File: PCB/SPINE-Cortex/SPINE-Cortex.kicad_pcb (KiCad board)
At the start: 2 copper layers, 49 x 49 mm, 78 parts, among them J1 SWD, J2 Conn_01x08, J3 Conn_01x02, J4 CAN_IN, J5 CAN_OUT, U1 STM32F103C8Tx, U4 MIC5219-3.3YM5, U5 TCAN1044V, U7 TPS54240DGQ, Y1 Resonator

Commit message: Finish Vertebra
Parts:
- removed C6: 100nF, Capacitor_SMD:C_0603_1608Metric
- removed J3: Conn_01x02, Connector_PinHeader_2.00mm:PinHeader_1x02_P2.00mm_Vertical
- removed R17: 10K, Resistor_SMD:R_0603_1608Metric
- added C1: 100nF, Capacitor_SMD:C_0603_1608Metric, F.Cu at (93.1, 117.6)
- added R16: 120R, Resistor_SMD:R_0603_1608Metric, F.Cu at (90.1, 117.6)
- added U3: SP3485EN, Package_SO:SOIC-8_3.9x4.9mm_P1.27mm, F.Cu at (90.1, 113.1)
- J2: value Conn_01x08 -> Conn_01x06; footprint Connector_JST:JST_GH_SM08B-GHS-TB_1x08-1MP_P1.25mm_Horizontal -> Connector_JST:JST_GH_SM06B-GHS-TB_1x06-1MP_P1.25mm_Horizontal
- U1: value STM32F103C8Tx -> STM32G431RBTx; footprint Package_QFP:LQFP-48_7x7mm_P0.5mm -> Package_QFP:LQFP-64_10x10mm_P0.5mm
- moved C16 58.4 mm to (99.6, 108.0)
- moved U4 58.4 mm to (96.0, 107.2)
- moved C17 55.7 mm to (99.6, 106.3), turned to 0 degrees
- moved C8 50.4 mm to (82.5, 104.2)
- moved D4 50.4 mm to (79.0, 101.4)
- moved R1 50.4 mm to (82.5, 102.7)
- moved R15 50.4 mm to (92.5, 102.2)
- moved R2 50.4 mm to (82.5, 101.2)
- moved R3 50.4 mm to (85.5, 104.2)
- moved R4 50.4 mm to (91.5, 104.2)
- moved R5 50.4 mm to (88.5, 104.2)
- moved C14 50.4 mm to (92.5, 100.6)
- moved C2 50.4 mm to (84.4, 97.6)
- moved C11 50.4 mm to (94.8, 101.4)
- moved C15 50.4 mm to (87.7, 98.8)
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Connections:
- J2 pad 1: unconnected-(J2-Pin_1-Pad1) -> GND
- J2 pad 2: unconnected-(J2-Pin_2-Pad2) -> +5V
- J2 pad 3: unconnected-(J2-Pin_3-Pad3) -> RS485_A
- J2 pad 4: unconnected-(J2-Pin_4-Pad4) -> RS485_B
- J2 pad 5: unconnected-(J2-Pin_5-Pad5) -> FAULT
- J2 pad 6: unconnected-(J2-Pin_6-Pad6) -> ENABLE
- U1 pad 15: unconnected-(U1-PA5-Pad15) -> GND
- U1 pad 16: unconnected-(U1-PA6-Pad16) -> +3.3V
- U1 pad 23: GND -> unconnected-(U1-PC5-Pad23)
- U1 pad 24: +3.3V -> unconnected-(U1-PB0-Pad24)
- U1 pad 27: unconnected-(U1-PB14-Pad27) -> GND
- U1 pad 28: unconnected-(U1-PB15-Pad28) -> Reset
- U1 pad 29: unconnected-(U1-PA8-Pad29) -> VREF
- U1 pad 31: unconnected-(U1-PA10-Pad31) -> GND
- U1 pad 32: CANRX -> +3.3V
- U1 pad 33: CANTX -> unconnected-(U1-PB11-Pad33)
- U1 pad 34: SWDIO -> unconnected-(U1-PB12-Pad34)
- U1 pad 35: GND -> unconnected-(U1-PB13-Pad35)
- U1 pad 36: +3.3V -> unconnected-(U1-PB14-Pad36)
- U1 pad 37: SWCLK -> unconnected-(U1-PB15-Pad37)
- U1 pad 44: BOOT -> unconnected-(U1-PA10-Pad44)
- U1 pad 45: unconnected-(U1-PB8-Pad45) -> CANRX
- U1 pad 46: unconnected-(U1-PB9-Pad46) -> CANTX
- U1 pad 7: Reset -> BOOT
- U1 pad 8: GND -> unconnected-(U1-PC0-Pad8)
- U1 pad 9: VREF -> unconnected-(U1-PC1-Pad9)
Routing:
- added copper zone on B.Cu, net GND

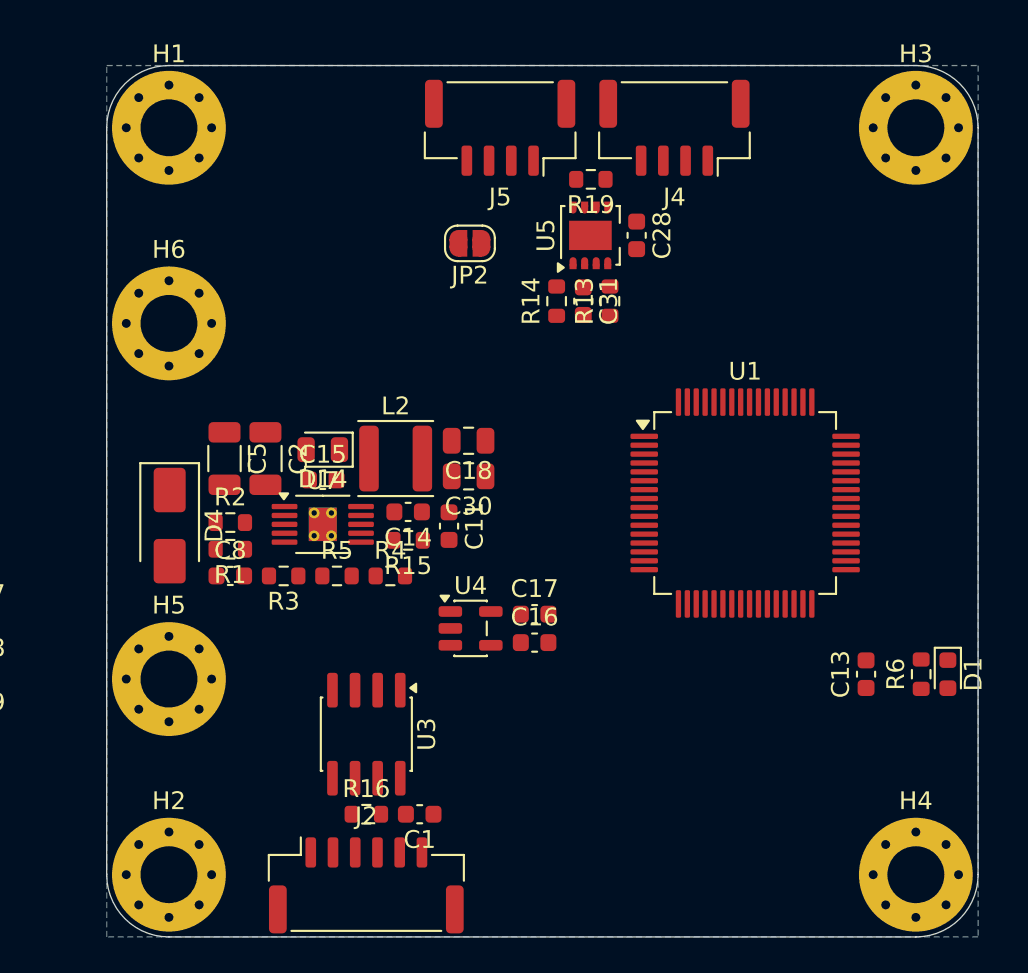
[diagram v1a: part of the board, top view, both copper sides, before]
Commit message: Vertebra fix
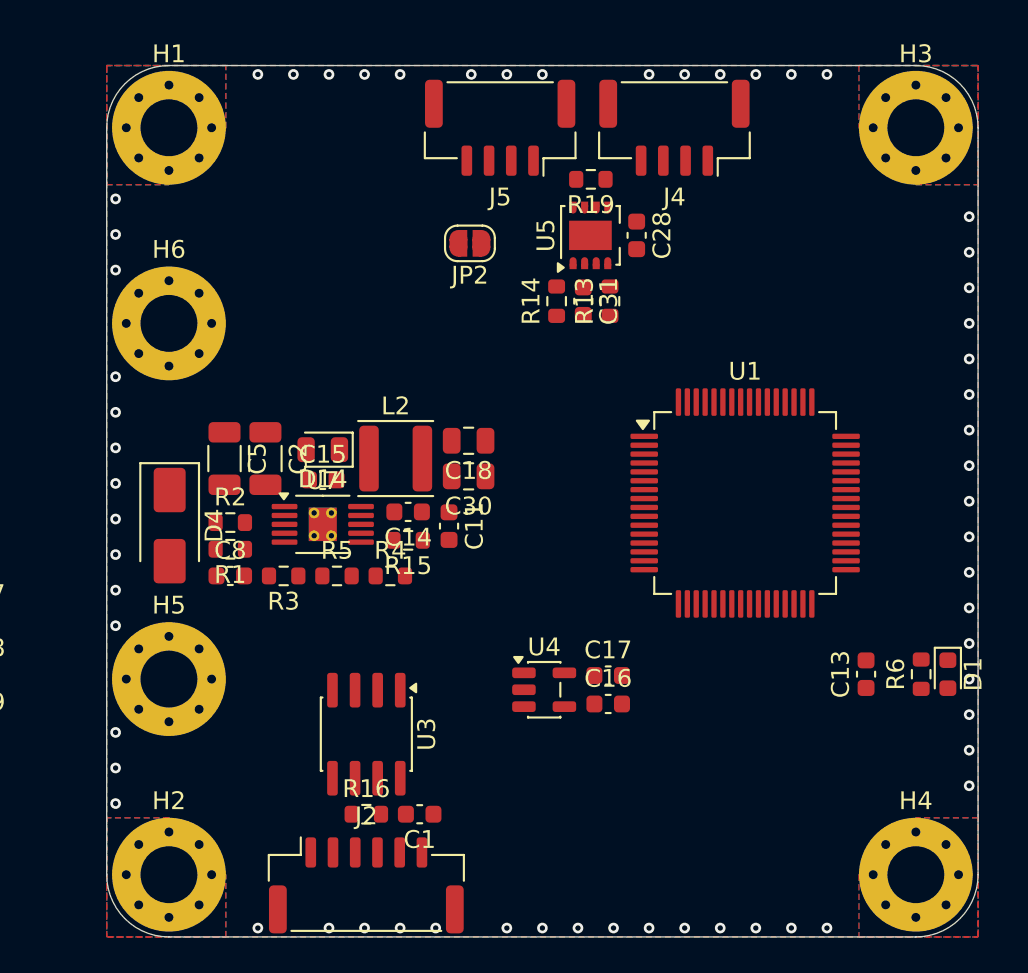
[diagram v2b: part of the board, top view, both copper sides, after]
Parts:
- moved C16 5.39 mm to (103.7, 111.4)
- moved C17 5.39 mm to (103.7, 109.8)
- moved U4 5.39 mm to (100.1, 110.6)
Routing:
- net GND: vias 0 -> 60
- added copper zone on F.Cu, net GND
- added copper zone on B.Cu, net unconnected-(H1-Pad1)
- added copper zone on F.Cu, net unconnected-(H1-Pad1)
- added copper zone on B.Cu, net unconnected-(H2-Pad1)
- added copper zone on F.Cu, net unconnected-(H2-Pad1)
- added copper zone on B.Cu, net unconnected-(H3-Pad1)
- added copper zone on F.Cu, net unconnected-(H3-Pad1)
- added copper zone on B.Cu, net unconnected-(H4-Pad1)
- added copper zone on F.Cu, net unconnected-(H4-Pad1)

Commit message: update
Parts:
- removed C4: 100nF, Capacitor_SMD:C_0603_1608Metric
- removed C45: 10uF, Capacitor_SMD:C_1206_3216Metric
- removed TH1: Thermistor_NTC, Resistor_SMD:R_0603_1608Metric
- added BZ1: Buzzer, Buzzer_Beeper:Buzzer_12x9.5RM7.6, F.Cu at (56.7, 82.0)
- added C3: 100nF, Capacitor_SMD:C_0603_1608Metric, F.Cu at (116.1, 111.8)
- added C6: 100nF, Capacitor_SMD:C_0603_1608Metric, F.Cu at (120.9, 107.9)
- added D2: B5819WS, Diode_SMD:D_0805_2012Metric, F.Cu at (57.0, 90.3)
- added D3: WS2812B-2020, LED_SMD:LED_WS2812B-2020_PLCC4_2.0x2.0mm, F.Cu at (110.6, 78.5)
- added J3: Conn_01x02, Connector_PinHeader_2.00mm:PinHeader_1x02_P2.00mm_Vertical, F.Cu at (121.6, 112.8)
- added J6: CAN_IN, Connector_JST:JST_GH_SM04B-GHS-TB_1x04-1MP_P1.25mm_Horizontal, F.Cu at (118.2, 58.0)
- added J7: Conn_01x02, TerminalBlock_MetzConnect:TerminalBlock_MetzConnect_Type094_RT03502HBLU_1x02_P5.00mm_Horizontal, F.Cu at (119.7, 85.9)
- added Q1: Q_NMOS_GSD, Package_TO_SOT_SMD:SOT-23, F.Cu at (61.0, 90.3)
- added Q2: Q_NMOS_GSD, Package_TO_SOT_SMD:SOT-23, F.Cu at (110.5, 56.5)
- added Q3: Q_NMOS_GSD, Package_TO_SOT_SMD:SOT-23, F.Cu at (110.5, 61.0)
- added Q4: Q_NMOS_GSD, Package_TO_SOT_SMD:SOT-23, F.Cu at (110.5, 65.5)
- added Q7: Q_PMOS_GSD, Package_TO_SOT_SMD:SOT-23, F.Cu at (107.2, 120.0)
- added Q8: Q_NMOS_GSD, Package_TO_SOT_SMD:SOT-23, F.Cu at (110.4, 118.2)
- added R17: 10K, Resistor_SMD:R_0603_1608Metric, F.Cu at (63.7, 90.3)
- added R18: 10K, Resistor_SMD:R_0603_1608Metric, F.Cu at (112.9, 120.2)
- added R20: 10K, Resistor_SMD:R_0603_1608Metric, F.Cu at (66.4, 91.1)
- added R21: 1K, Resistor_SMD:R_0603_1608Metric, F.Cu at (108.6, 92.8)
- added R22: 10K, Resistor_SMD:R_0603_1608Metric, F.Cu at (107.2, 117.3)
- added R23: 220R, Resistor_SMD:R_0603_1608Metric, F.Cu at (108.7, 84.4)
- added R24: 1K, Resistor_SMD:R_0603_1608Metric, F.Cu at (103.8, 117.6)
- added R26: 10K, Resistor_SMD:R_0603_1608Metric, F.Cu at (110.4, 120.9)
- added U2: STM32G431RBTx, Package_QFP:LQFP-64_10x10mm_P0.5mm, F.Cu at (110.4, 105.8)
- U1: value STM32G431RBTx -> SFH617A-2X009T; footprint Package_QFP:LQFP-64_10x10mm_P0.5mm -> Package_DIP:SMDIP-4_W9.53mm_Clearance8mm
- moved C7 74.9 mm to (111.1, 114.1), turned to 90 degrees
- moved C23 74.2 mm to (116.4, 100.1), turned to 90 degrees
- moved C9 72.4 mm to (109.6, 114.1), turned to 90 degrees
- moved R10 71.0 mm to (120.9, 109.4)
- moved FB1 69.2 mm to (113.4, 113.3), turned to 180 degrees
- moved Y1 68.3 mm to (101.4, 103.8), turned to -90 degrees
- moved C26 63.3 mm to (104.7, 98.3), turned to 180 degrees
- moved C21 62.9 mm to (104.4, 111.5), turned to -90 degrees
- moved J1 62.8 mm to (121.4, 104.6), turned to 180 degrees
- moved C24 62.8 mm to (104.7, 99.8), turned to 180 degrees
- moved C19 59.8 mm to (101.4, 108.3)
- moved R9 57.4 mm to (107.7, 98.3)
- moved R7 52.7 mm to (101.4, 106.8), turned to 180 degrees
- moved C18 48.5 mm to (48.8, 108.6), turned to -90 degrees
- moved C34 47.3 mm to (79.0, 95.4)
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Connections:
- C2 pad 2: Net-(D4-K) -> VDC
- C5 pad 2: Net-(D4-K) -> VDC
- D4 pad 1: Net-(D4-K) -> VDC
- D4 pad 2: VDC -> PRI_HI
- H5 pad 1: VDC -> PRI_HI
- J2 pad 5: FAULT -> ENABLE
- J2 pad 6: ENABLE -> FAULT
- R2 pad 2: Net-(D4-K) -> VDC
- U1 pad 1: +3.3V -> Net-(J7-Pin_1)
- U1 pad 2: unconnected-(U1-PC13-Pad2) -> Net-(R23-Pad1)
- U1 pad 3: unconnected-(U1-PC14-Pad3) -> TIM_BKIN_1
- U1 pad 4: unconnected-(U1-PC15-Pad4) -> +3.3V
- U7 pad 2: Net-(D4-K) -> VDC
- Y1 pad 1: Net-(U1-PF0) -> Net-(U2-PF0)
- Y1 pad 3: Net-(U1-PF1) -> Net-(U2-PF1)
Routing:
- net Net-(J7-Pin_1): track 0.00 -> 6.96 mm
- net Net-(Q7-G): track 0.00 -> 4.20 mm
- net +5V: track 0.00 -> 1.81 mm
- net Net-(Q8-G): track 0.00 -> 1.81 mm
- net GND: vias 60 -> 58

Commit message: update
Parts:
- removed C43, C44: 10uF, Capacitor_SMD:C_1206_3216Metric
- removed D6: LED_RBAG, LED_SMD:LED_Cree-PLCC4_2x2mm_CW
- removed J1: SWD, Connector_PinHeader_2.54mm:PinHeader_1x03_P2.54mm_Vertical
- removed Q2, Q3, Q4: Q_NMOS_GSD, Package_TO_SOT_SMD:SOT-23
- removed R11, R12, R8: 1K, Resistor_SMD:R_0603_1608Metric
- added C4: 100nF, Capacitor_SMD:C_0603_1608Metric, F.Cu at (84.9, 109.4)
- added D5: LED_Small, LED_SMD:LED_0603_1608Metric, F.Cu at (83.3, 123.0)
- added D7: B5819WS, Diode_SMD:D_0805_2012Metric, F.Cu at (88.2, 87.1)
- added J9: Conn_02x03_Odd_Even, Connector_PinHeader_2.54mm:PinHeader_2x03_P2.54mm_Vertical, F.Cu at (103.5, 119.3)
- added R25: 1K, Resistor_SMD:R_0603_1608Metric, F.Cu at (83.3, 120.0)
- BZ1: footprint Buzzer_Beeper:Buzzer_12x9.5RM7.6 -> Buzzer_Beeper:MagneticBuzzer_CUI_CMT-8504-100-SMT
- J3: footprint Connector_PinHeader_2.00mm:PinHeader_1x02_P2.00mm_Vertical -> Connector_PinHeader_2.54mm:PinHeader_1x02_P2.54mm_Vertical
- moved J6 78.7 mm to (98.7, 134.3)
- moved J5 76.2 mm to (120.4, 131.6), turned to 0 degrees
- moved U3 74.3 mm to (137.3, 118.9)
- moved C1 74.3 mm to (140.8, 121.1)
- moved R16 73.4 mm to (137.3, 123.4)
- moved J4 70.2 mm to (110.9, 131.6), turned to 0 degrees
- moved TP1 66.4 mm to (110.3, 60.6)
- moved TP2 66.4 mm to (110.3, 63.6)
- moved TP3 66.4 mm to (110.3, 66.7)
- moved TP4 66.4 mm to (113.3, 60.6)
- moved TP5 66.4 mm to (113.3, 63.6)
- moved TP6 66.4 mm to (113.3, 66.7)
- moved TP7 66.4 mm to (116.4, 60.6)
- moved TP8 66.4 mm to (116.4, 63.6)
- moved TP9 66.4 mm to (116.4, 66.7)
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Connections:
- BZ1 pad 1: +5V -> Net-(BZ1-+)
- D2 pad 1: +5V -> Net-(BZ1-+)
- D3 pad 2: unconnected-(D3-VSS-Pad2) -> GND
- D3 pad 3: unconnected-(D3-DIN-Pad3) -> LED1
- D3 pad 4: unconnected-(D3-VDD-Pad4) -> +5V
- R21 pad 2: TIM_BKIN_1 -> TIM_BKIN_2
- R6 pad 1: +3.3V -> +5V
- U1 pad 3: TIM_BKIN_1 -> TIM_BKIN_2
- U2 pad 13: unconnected-(U2-PA1-Pad13) -> USART2_DE
- U2 pad 14: unconnected-(U2-PA2-Pad14) -> USART2_TX
- U2 pad 17: unconnected-(U2-PA3-Pad17) -> USART2_RX
- U2 pad 20: unconnected-(U2-PA6-Pad20) -> FAULT
- U2 pad 59: unconnected-(U2-PB6-Pad59) -> TIM_BKIN_2
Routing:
- net VDC: track 0.00 -> 24.3 mm
- net +5V: track 1.81 -> 8.52 mm
- net VREF: track 0.00 -> 5.51 mm
- net PRI_HI: track 0.00 -> 5.50 mm
- net Net-(BZ1-+): track 0.00 -> 5.44 mm
- net +3.3V: track 0.00 -> 5.11 mm
- net Net-(U7-VSENSE): track 0.00 -> 4.96 mm
- net Net-(U7-EN): track 0.00 -> 4.93 mm
- net Net-(U7-COMP): track 0.00 -> 3.79 mm
- net Net-(U7-RT/CLK): track 0.00 -> 3.21 mm
- net Net-(BZ1--): track 0.00 -> 2.92 mm
- net TIM_BKIN_2: track 0.00 -> 2.75 mm
- net Net-(U7-SS/TR): track 0.00 -> 2.54 mm
- net Net-(R23-Pad1): track 0.00 -> 2.44 mm
- net Net-(Q7-G): track 4.20 -> 1.81 mm
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- added copper zone on F.Cu, net +5V
- added copper zone on F.Cu, net Net-(D14-K)
- added copper zone on F.Cu, net Net-(U7-BOOT)
- added copper zone on F.Cu, net VDC
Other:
- board text added: "3V3"
- board text added: "CLK"
- board text added: "DIO"
- board text added: "GND"
- board text added: "RXD"
- board text added: "TXD"

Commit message: update
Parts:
- removed C13: 10uF, Capacitor_SMD:C_0603_1608Metric
- removed J9: Conn_02x03_Odd_Even, Connector_PinHeader_2.54mm:PinHeader_2x03_P2.54mm_Vertical
- added C10: 100nF, Capacitor_SMD:C_0603_1608Metric, F.Cu at (103.6, 117.2)
- added J1: Conn_01x02, Connector_PinHeader_2.54mm:PinHeader_1x02_P2.54mm_Vertical, F.Cu at (103.6, 122.4)
- added J8: Conn_01x03, Connector_PinHeader_2.54mm:PinHeader_1x03_P2.54mm_Vertical, B.Cu at (97.0, 95.5)
- added R8: 10K, Resistor_SMD:R_0603_1608Metric, F.Cu at (103.6, 115.7)
- added SW1: SW_Push, Button_Switch_SMD:SW_SPST_B3S-1000, F.Cu at (120.8, 93.0)
- added SW2: SW_Push, Button_Switch_SMD:SW_SPST_B3S-1000, F.Cu at (120.8, 103.5)
- moved J5 60.8 mm to (90.0, 79.0), turned to 180 degrees
- moved J4 53.7 mm to (100.0, 79.0), turned to 180 degrees
- moved R19 51.1 mm to (83.9, 80.6), turned to -90 degrees
- moved JP2 49.8 mm to (83.9, 77.4)
- moved U5 46.0 mm to (101.5, 86.0), turned to 90 degrees
- moved C28 44.4 mm to (104.1, 86.0), turned to -90 degrees
- moved R14 42.5 mm to (100.0, 89.8), turned to 90 degrees
- moved C31 41.4 mm to (101.5, 89.8), turned to -90 degrees
- moved R13 40.3 mm to (103.0, 89.8), turned to 90 degrees
- moved J3 39.8 mm to (99.9, 122.4)
- moved C6 36.2 mm to (99.9, 117.2), turned to 0 degrees
- moved R10 35.0 mm to (99.9, 115.7), turned to 0 degrees
- moved Q8 29.2 mm to (119.9, 111.8), turned to 180 degrees
- moved R16 29.1 mm to (109.1, 116.2), turned to 90 degrees
- moved R18 28.9 mm to (120.5, 109.3)
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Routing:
- net +5V: track 8.52 -> 135.5 mm, vias 0 -> 2
- net +3.3V: track 5.11 -> 67.9 mm
- net ENABLE: track 0.00 -> 15.2 mm
- net FAULT: track 0.00 -> 12.0 mm
- net USART2_DE: track 0.00 -> 11.2 mm
- net RS485_B: track 0.00 -> 9.43 mm
- net CAN_L: track 0.00 -> 9.21 mm
- net Net-(Q8-G): track 0.00 -> 8.31 mm
- net USART2_RX: track 0.00 -> 8.08 mm
- net CANTX: track 0.00 -> 7.92 mm
- net RS485_A: track 0.00 -> 6.67 mm
- net USART2_TX: track 0.00 -> 5.92 mm
- net CANRX: track 0.00 -> 5.80 mm
- net Reset: track 0.00 -> 5.72 mm
- net VREF: track 5.51 -> 0.00 mm
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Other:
- board text added: "BOOT"
- board text added: "NTC1"
- board text added: "NTC2"
- board text removed: "3V3"
- board text removed: "RXD"
- board text removed: "TXD"

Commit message: update
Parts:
- removed TP6: TestPoint, TestPoint:TestPoint_Pad_D1.0mm
- added C12: 100nF, Capacitor_SMD:C_0603_1608Metric, F.Cu at (88.3, 115.0)
- added R11: 147K, Resistor_SMD:R_0603_1608Metric, F.Cu at (86.7, 113.3)
- added R12: 10K, Resistor_SMD:R_0603_1608Metric, F.Cu at (89.9, 113.3)
- D1, D5: value LED_Small -> LED
- moved TP2 50.4 mm to (106.1, 113.9)
- moved TP4 49.5 mm to (96.2, 107.0)
- moved TP5 49.3 mm to (93.9, 109.0)
- moved TP1 49.2 mm to (93.9, 107.0)
- moved TP3 44.6 mm to (96.2, 109.0)
- moved TP7 35.2 mm to (106.1, 94.3)
- moved TP8 31.2 mm to (104.1, 92.3)
- moved TP9 30.2 mm to (104.0, 94.3)
- moved R24 11.6 mm to (113.0, 105.7), turned to -90 degrees
- moved R7 6.31 mm to (101.7, 113.7), turned to 180 degrees
- moved R10 1.13 mm to (99.1, 114.9), turned to 90 degrees
- moved R8 1.06 mm to (104.3, 114.9), turned to 90 degrees
- moved J4 0.60 mm to (100.0, 78.4)
- moved J5 0.60 mm to (90.0, 78.4)
- moved C21 0.42 mm to (111.5, 107.7), turned to -90 degrees
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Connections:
- D3 pad 1: unconnected-(D3-DOUT-Pad1) -> Net-(D3-DOUT)
- J6 pad 1: unconnected-(J6-Pin_1-Pad1) -> GND
- J6 pad 2: unconnected-(J6-Pin_2-Pad2) -> +5V
- J6 pad 3: unconnected-(J6-Pin_3-Pad3) -> LED1
- J6 pad 4: unconnected-(J6-Pin_4-Pad4) -> Net-(D3-DOUT)
- JP2 pad 1: CAN_L -> CAN_H
- R19 pad 2: CAN_H -> CAN_L
- SW1 pad 1: unconnected-(SW1-Pad1) -> BUTTON_2
- SW2 pad 1: unconnected-(SW2-Pad1) -> BUTTON_1
- TP7 pad 1: unconnected-(TP7-Pad1) -> GND
- TP8 pad 1: unconnected-(TP8-Pad1) -> USART1_TX
- TP9 pad 1: unconnected-(TP9-Pad1) -> USART1_RX
- U2 pad 10: unconnected-(U2-PC2-Pad10) -> V_SENSE
- U2 pad 11: unconnected-(U2-PC3-Pad11) -> NTC_1
- U2 pad 12: unconnected-(U2-PA0-Pad12) -> NTC_2
- U2 pad 25: unconnected-(U2-PB1-Pad25) -> BUTTON_1
- U2 pad 26: unconnected-(U2-PB2-Pad26) -> BUTTON_2
- U2 pad 34: LED1 -> unconnected-(U2-PB12-Pad34)
- U2 pad 35: LED2 -> unconnected-(U2-PB13-Pad35)
- U2 pad 36: LED3 -> unconnected-(U2-PB14-Pad36)
- U2 pad 40: unconnected-(U2-PC8-Pad40) -> VERTEBRA_EN
- U2 pad 41: unconnected-(U2-PC9-Pad41) -> TIM_BKIN_2
- U2 pad 59: TIM_BKIN_2 -> unconnected-(U2-PB6-Pad59)
- U2 pad 62: unconnected-(U2-PB9-Pad62) -> LED1
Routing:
- net +3.3V: track 67.9 -> 116.3 mm
- net LED1: track 0.00 -> 29.8 mm
- net V_SENSE: track 0.00 -> 26.9 mm, vias 0 -> 2
- net VERTEBRA_EN: track 0.00 -> 25.7 mm, vias 0 -> 2
- net CAN_H: track 0.00 -> 25.5 mm, vias 0 -> 2
- net BUTTON_2: track 0.00 -> 18.4 mm
- net BUTTON_1: track 0.00 -> 16.5 mm
- net TIM_BKIN_2: track 2.75 -> 18.6 mm
- net NTC_1: track 4.48 -> 19.8 mm
- net CAN_L: track 9.21 -> 23.4 mm
- net Net-(D3-DOUT): track 0.00 -> 13.8 mm, vias 0 -> 2
- net NTC_2: track 4.48 -> 15.6 mm
- net FAULT: track 12.0 -> 21.1 mm
- net BOOT: track 1.94 -> 8.89 mm
- net Reset: track 5.72 -> 11.4 mm
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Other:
- board text added: "+"
- board text added: "3V3"
- board text added: "5V"
- board text added: "RST"
- board text added: "RX"
- board text added: "TX"
